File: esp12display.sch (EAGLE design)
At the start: 3 parts

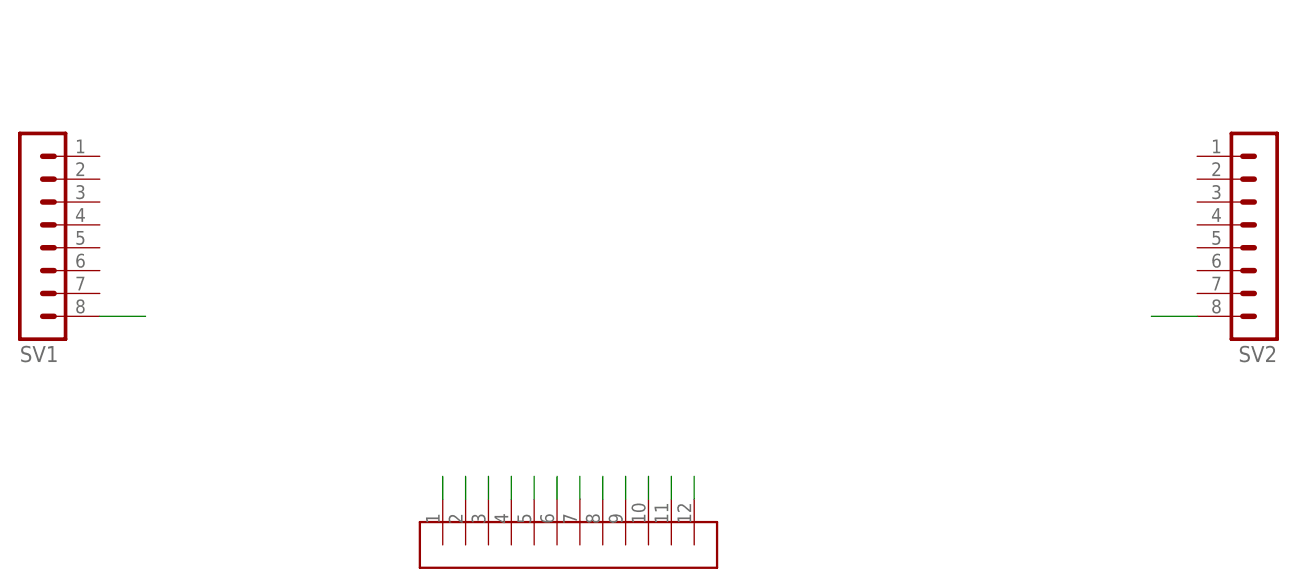
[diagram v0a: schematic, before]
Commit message: some major updates
* working ft232rl layout
* replaced the DIN resistors for the WS2112 with solder jumpers
* sensors breakout board
* fixed a bug (missing trace) in the rgbwwpw board
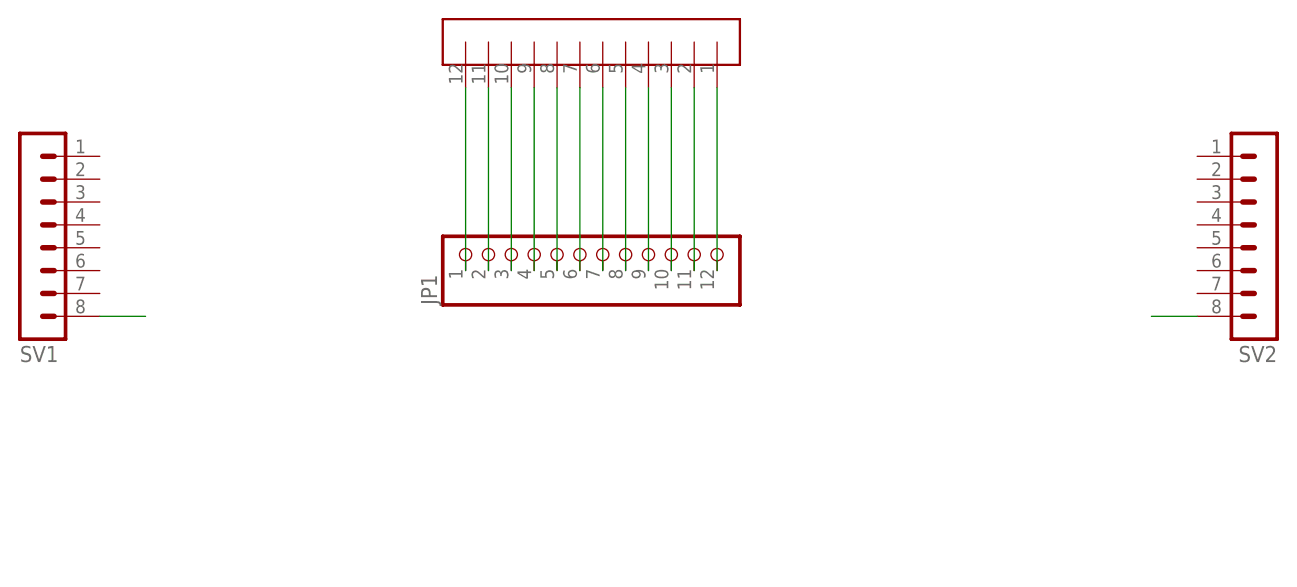
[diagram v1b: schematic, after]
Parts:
- removed U$2: 12PIN_LCD_PADS, 12Pin_LCD_Connector:12PIN_LCD_PADS
- added JP1: (no value), adafruit:PINHD-1X12
- added U$1: 12PIN_LCD_PADS, esp12display:12PIN_LCD_PADS
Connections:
- net N$10: now also JP1.9, U$1.P$4; no longer U$2.P$9
- net N$11: now also JP1.10, U$1.P$3; no longer U$2.P$10
- net N$12: now also JP1.11, U$1.P$2; no longer U$2.P$11
- net N$13: now also JP1.12, U$1.P$1; no longer U$2.P$12
- net N$2: now also JP1.1, U$1.P$12; no longer U$2.P$1
- net N$3: now also JP1.2, U$1.P$11; no longer U$2.P$2
- net N$4: now also JP1.3, U$1.P$10; no longer U$2.P$3
- net N$5: now also JP1.4, U$1.P$9; no longer U$2.P$4
- net N$6: now also JP1.5, U$1.P$8; no longer U$2.P$5
- net N$7: now also JP1.6, U$1.P$7; no longer U$2.P$6
- net N$8: now also JP1.7, U$1.P$6; no longer U$2.P$7
- net N$9: now also JP1.8, U$1.P$5; no longer U$2.P$8
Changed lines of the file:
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@@
 <part name="SV1" library="con-lstb" deviceset="MA08-1" device=""/>
 <part name="SV2" library="con-lstb" deviceset="MA08-1" device=""/>
-<part name="U$2" library="12Pin_LCD_Connector" deviceset="12PIN_LCD_PADS" device=""/>
+<part name="U$1" library="esp12display" deviceset="12PIN_LCD_PADS" device=""/>
+<part name="JP1" library="adafruit" deviceset="PINHD-1X12" device=""/>
 </parts>
 <sheets>
@@
 <instance part="SV1" gate="1" x="22.86" y="35.56" rot="MR180"/>
 <instance part="SV2" gate="1" x="160.02" y="35.56" rot="R180"/>
-<instance part="U$2" gate="G$1" x="86.36" y="30.48" rot="R90"/>
+<instance part="U$1" gate="G$1" x="81.28" y="25.4" rot="R270"/>
+<instance part="JP1" gate="G$1" x="83.82" y="33.02" rot="R90"/>
 </instances>
 <busses>
@@
 <net name="N$2" class="0">
 <segment>
-<pinref part="U$2" gate="G$1" pin="P$1"/>
-<wire x1="68.58" y1="5.08" x2="68.58" y2="7.62" width="0.1524" layer="91"/>
+<pinref part="U$1" gate="G$1" pin="P$12"/>
+<pinref part="JP1" gate="G$1" pin="1"/>
+<wire x1="71.12" y1="50.8" x2="71.12" y2="30.48" width="0.1524" layer="91"/>
 </segment>
 </net>
 <net name="N$3" class="0">
 <segment>
-<pinref part="U$2" gate="G$1" pin="P$2"/>
-<wire x1="71.12" y1="5.08" x2="71.12" y2="7.62" width="0.1524" layer="91"/>
+<pinref part="U$1" gate="G$1" pin="P$11"/>
+<pinref part="JP1" gate="G$1" pin="2"/>
+<wire x1="73.66" y1="50.8" x2="73.66" y2="30.48" width="0.1524" layer="91"/>
 </segment>
 </net>
 <net name="N$4" class="0">
 <segment>
-<pinref part="U$2" gate="G$1" pin="P$3"/>
-<wire x1="73.66" y1="5.08" x2="73.66" y2="7.62" width="0.1524" layer="91"/>
+<pinref part="U$1" gate="G$1" pin="P$10"/>
+<pinref part="JP1" gate="G$1" pin="3"/>
+<wire x1="76.2" y1="50.8" x2="76.2" y2="30.48" width="0.1524" layer="91"/>
 </segment>
 </net>
 <net name="N$5" class="0">
 <segment>
-<pinref part="U$2" gate="G$1" pin="P$4"/>
-<wire x1="76.2" y1="5.08" x2="76.2" y2="7.62" width="0.1524" layer="91"/>
+<pinref part="U$1" gate="G$1" pin="P$9"/>
+<pinref part="JP1" gate="G$1" pin="4"/>
+<wire x1="78.74" y1="50.8" x2="78.74" y2="30.48" width="0.1524" layer="91"/>
 </segment>
 </net>
 <net name="N$6" class="0">
 <segment>
-<pinref part="U$2" gate="G$1" pin="P$5"/>
-<wire x1="78.74" y1="5.08" x2="78.74" y2="7.62" width="0.1524" layer="91"/>
+<pinref part="U$1" gate="G$1" pin="P$8"/>
+<pinref part="JP1" gate="G$1" pin="5"/>
+<wire x1="81.28" y1="50.8" x2="81.28" y2="30.48" width="0.1524" layer="91"/>
 </segment>
 </net>
 <net name="N$7" class="0">
 <segment>
-<pinref part="U$2" gate="G$1" pin="P$6"/>
-<wire x1="81.28" y1="5.08" x2="81.28" y2="7.62" width="0.1524" layer="91"/>
+<pinref part="U$1" gate="G$1" pin="P$7"/>
+<pinref part="JP1" gate="G$1" pin="6"/>
+<wire x1="83.82" y1="50.8" x2="83.82" y2="30.48" width="0.1524" layer="91"/>
 </segment>
 </net>
 <net name="N$8" class="0">
 <segment>
-<pinref part="U$2" gate="G$1" pin="P$7"/>
-<wire x1="83.82" y1="5.08" x2="83.82" y2="7.62" width="0.1524" layer="91"/>
+<pinref part="U$1" gate="G$1" pin="P$6"/>
+<pinref part="JP1" gate="G$1" pin="7"/>
+<wire x1="86.36" y1="50.8" x2="86.36" y2="30.48" width="0.1524" layer="91"/>
 </segment>
 </net>
 <net name="N$9" class="0">
 <segment>
-<pinref part="U$2" gate="G$1" pin="P$8"/>
-<wire x1="86.36" y1="7.62" x2="86.36" y2="5.08" width="0.1524" layer="91"/>
+<pinref part="U$1" gate="G$1" pin="P$5"/>
+<pinref part="JP1" gate="G$1" pin="8"/>
+<wire x1="88.9" y1="50.8" x2="88.9" y2="30.48" width="0.1524" layer="91"/>
 </segment>
 </net>
 <net name="N$10" class="0">
 <segment>
-<pinref part="U$2" gate="G$1" pin="P$9"/>
-<wire x1="88.9" y1="5.08" x2="88.9" y2="7.62" width="0.1524" layer="91"/>
+<pinref part="U$1" gate="G$1" pin="P$4"/>
+<pinref part="JP1" gate="G$1" pin="9"/>
+<wire x1="91.44" y1="50.8" x2="91.44" y2="30.48" width="0.1524" layer="91"/>
 </segment>
 </net>
 <net name="N$11" class="0">
 <segment>
-<pinref part="U$2" gate="G$1" pin="P$10"/>
-<wire x1="91.44" y1="5.08" x2="91.44" y2="7.62" width="0.1524" layer="91"/>
+<pinref part="U$1" gate="G$1" pin="P$3"/>
+<pinref part="JP1" gate="G$1" pin="10"/>
+<wire x1="93.98" y1="50.8" x2="93.98" y2="30.48" width="0.1524" layer="91"/>
 </segment>
 </net>
 <net name="N$12" class="0">
 <segment>
-<pinref part="U$2" gate="G$1" pin="P$11"/>
-<wire x1="93.98" y1="5.08" x2="93.98" y2="7.62" width="0.1524" layer="91"/>
+<pinref part="U$1" gate="G$1" pin="P$2"/>
+<pinref part="JP1" gate="G$1" pin="11"/>
+<wire x1="96.52" y1="50.8" x2="96.52" y2="30.48" width="0.1524" layer="91"/>
 </segment>
 </net>
 <net name="N$13" class="0">
 <segment>
-<pinref part="U$2" gate="G$1" pin="P$12"/>
-<wire x1="96.52" y1="5.08" x2="96.52" y2="7.62" width="0.1524" layer="91"/>
+<pinref part="U$1" gate="G$1" pin="P$1"/>
+<pinref part="JP1" gate="G$1" pin="12"/>
+<wire x1="99.06" y1="50.8" x2="99.06" y2="30.48" width="0.1524" layer="91"/>
 </segment>
 </net>
